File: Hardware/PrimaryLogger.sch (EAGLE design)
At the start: 72 parts, among them J1 CONN_42.54_SCREW, J2 CONN_42.54_SCREW, J3 CONN_42.54_SCREW, J4 CONN_42.54_SCREW, J5 CONN_32.54_SCREW, Q1 DMG3404, Q2 DMG3404, U1 MIC2005, U2 MIC2005, U25 SN74AUP3G34DCU, U3 TPL5010DDC, U4 TXS0102DCU, U5 SN74LVC1G3157SC70, U6 TCS3400, U7 SHTC3DFN, U8 MCP23008QFN, U9 MCP7940SOIC

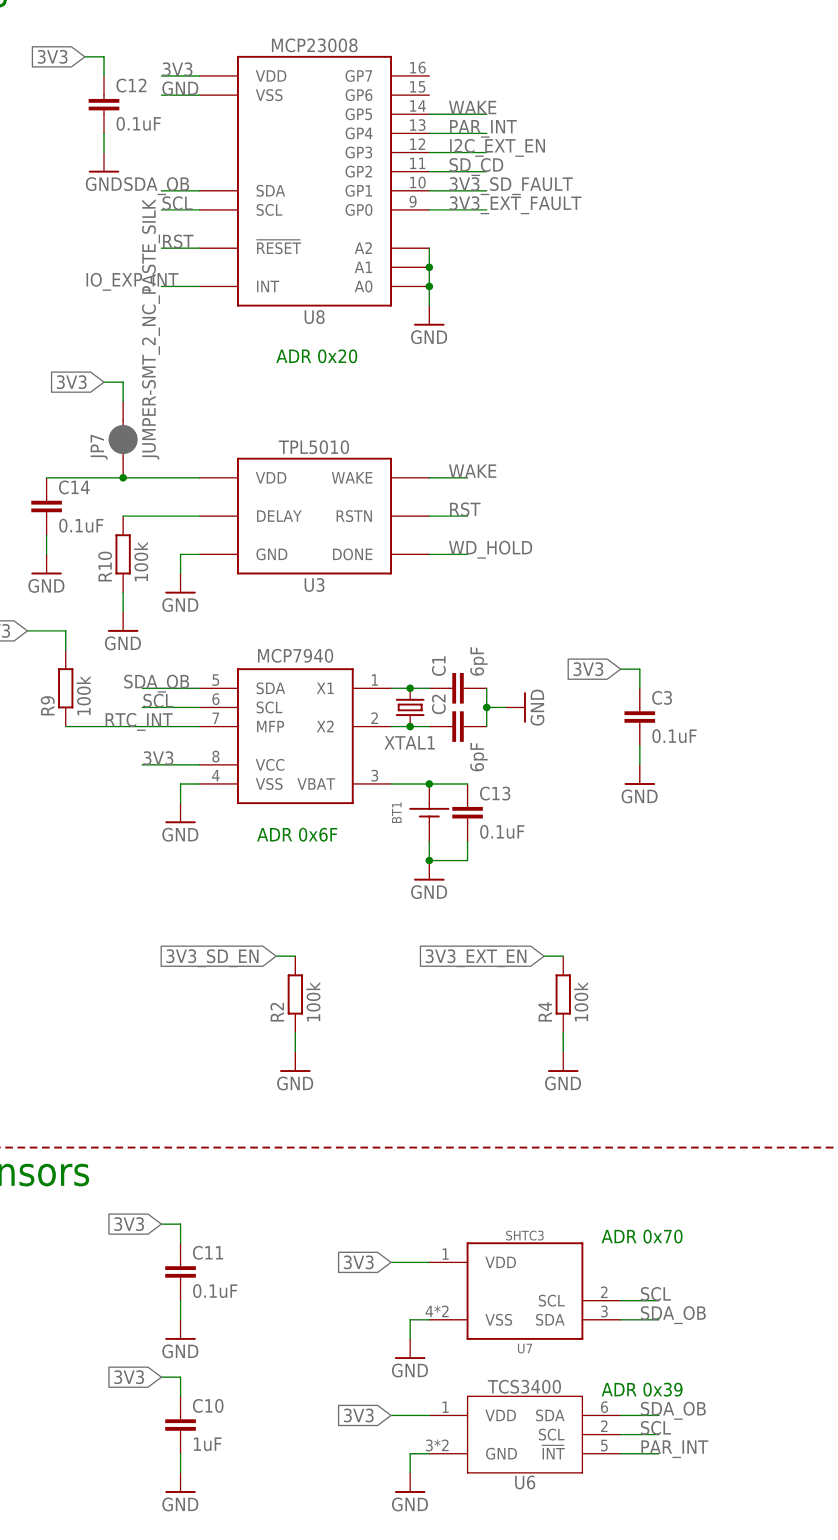
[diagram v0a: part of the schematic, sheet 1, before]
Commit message: Documentation and folder structure updates
Moved around the folder structure, added board pictures, and added to README
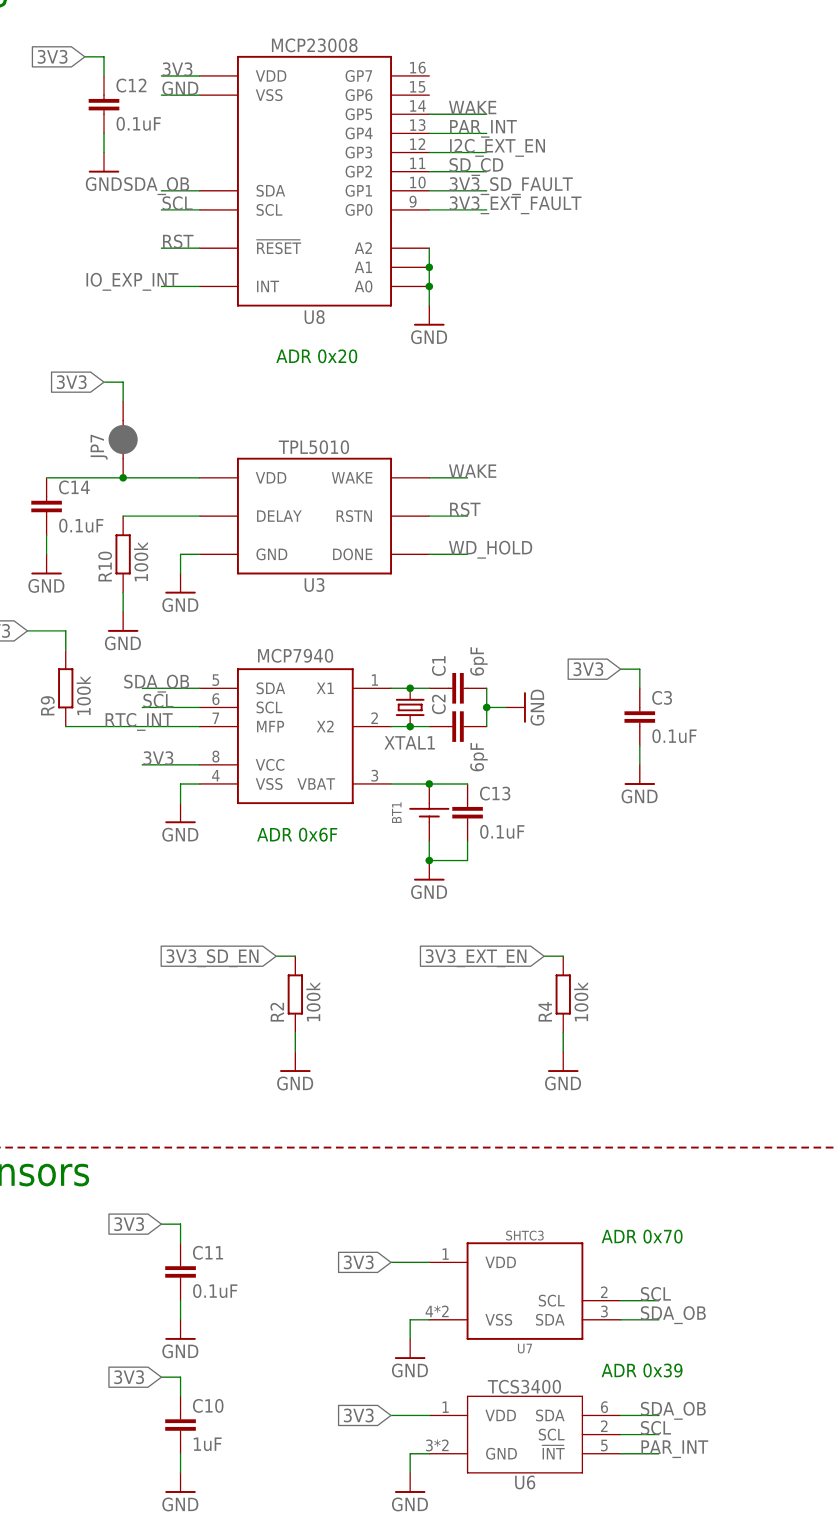
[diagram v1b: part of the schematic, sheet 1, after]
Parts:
- JP1, JP2, JP3, JP4, JP5, JP6, JP8: device bschulz:JUMPER-SMT_3_1-NC_PASTE_SILK -> SparkFun-Jumpers:JUMPER-SMT_3_1-NC_PASTE_SILK
- JP10: device bschulz:JUMPER-SMT_2_NO_SILK -> SparkFun-Jumpers:JUMPER-SMT_2_NO_SILK
- JP7, JP9: device bschulz:JUMPER-SMT_2_NC_PASTE_SILK -> SparkFun-Jumpers:JUMPER-SMT_2_NC_PASTE_SILK
- R8: value 10k -> 100k
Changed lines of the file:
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@@
 <?xml version="1.0" encoding="utf-8"?>
 <!DOCTYPE eagle SYSTEM "eagle.dtd">
-<eagle version="9.5.2">
+<eagle version="9.6.2">
 <drawing>
 <settings>
@@
 <layer number="115" name="ReferenceISLANDS" color="7" fill="1" visible="no" active="yes"/>
 <layer number="116" name="Patch_BOT" color="7" fill="1" visible="no" active="yes"/>
-<layer number="117" name="PM_Ref" color="7" fill="1" visible="no" active="no"/>
 <layer number="118" name="Rect_Pads" color="7" fill="1" visible="no" active="yes"/>
-<layer number="119" name="PF_Ref" color="7" fill="1" visible="no" active="no"/>
-<layer number="120" name="WFL_Ref" color="7" fill="1" visible="no" active="no"/>
 <layer number="121" name="_tsilk" color="7" fill="1" visible="no" active="yes"/>
 <layer number="122" name="_bsilk" color="7" fill="1" visible="no" active="yes"/>
@@
 <part name="J3" library="bschulz" deviceset="CONN_4" device="2.54_SCREW"/>
 <part name="J4" library="bschulz" deviceset="CONN_4" device="2.54_SCREW"/>
-<part name="JP1" library="bschulz" deviceset="JUMPER-SMT_3_1-NC_PASTE" device="_SILK" package3d_urn="urn:adsk.eagle:package:39293/1"/>
-<part name="JP2" library="bschulz" deviceset="JUMPER-SMT_3_1-NC_PASTE" device="_SILK" package3d_urn="urn:adsk.eagle:package:39293/1"/>
-<part name="JP3" library="bschulz" deviceset="JUMPER-SMT_3_1-NC_PASTE" device="_SILK" package3d_urn="urn:adsk.eagle:package:39293/1"/>
-<part name="JP4" library="bschulz" deviceset="JUMPER-SMT_3_1-NC_PASTE" device="_SILK" package3d_urn="urn:adsk.eagle:package:39293/1"/>
-<part name="JP5" library="bschulz" deviceset="JUMPER-SMT_3_1-NC_PASTE" device="_SILK" package3d_urn="urn:adsk.eagle:package:39293/1"/>
-<part name="JP6" library="bschulz" deviceset="JUMPER-SMT_3_1-NC_PASTE" device="_SILK" package3d_urn="urn:adsk.eagle:package:39293/1"/>
+<part name="JP1" library="SparkFun-Jumpers" library_urn="urn:adsk.eagle:library:528" deviceset="JUMPER-SMT_3_1-NC_PASTE" device="_SILK" package3d_urn="urn:adsk.eagle:package:39293/1"/>
+<part name="JP2" library="SparkFun-Jumpers" library_urn="urn:adsk.eagle:library:528" deviceset="JUMPER-SMT_3_1-NC_PASTE" device="_SILK" package3d_urn="urn:adsk.eagle:package:39293/1"/>
+<part name="JP3" library="SparkFun-Jumpers" library_urn="urn:adsk.eagle:library:528" deviceset="JUMPER-SMT_3_1-NC_PASTE" device="_SILK" package3d_urn="urn:adsk.eagle:package:39293/1"/>
+<part name="JP4" library="SparkFun-Jumpers" library_urn="urn:adsk.eagle:library:528" deviceset="JUMPER-SMT_3_1-NC_PASTE" device="_SILK" package3d_urn="urn:adsk.eagle:package:39293/1"/>
+<part name="JP5" library="SparkFun-Jumpers" library_urn="urn:adsk.eagle:library:528" deviceset="JUMPER-SMT_3_1-NC_PASTE" device="_SILK" package3d_urn="urn:adsk.eagle:package:39293/1"/>
+<part name="JP6" library="SparkFun-Jumpers" library_urn="urn:adsk.eagle:library:528" deviceset="JUMPER-SMT_3_1-NC_PASTE" device="_SILK" package3d_urn="urn:adsk.eagle:package:39293/1"/>
 <part name="U5" library="bschulz" deviceset="SN74LVC1G3157" device="SC70" value="SN74LVC1G3157SC70"/>
 <part name="R6" library="bschulz_passives" deviceset="R-EU_" device="R0603" technology="100K" value="100k"/>
@@
 <part name="J5" library="bschulz" deviceset="CONN_3" device="2.54_SCREW"/>
 <part name="J6" library="bschulz" deviceset="CONN_02" device="2.54_SCREW_ROUND"/>
-<part name="R8" library="bschulz_passives" deviceset="R-EU_" device="R0603" technology="10K" value="10k"/>
+<part name="R8" library="bschulz_passives" deviceset="R-EU_" device="R0603" technology="10K" value="100k"/>
 <part name="J7" library="bschulz" deviceset="CONN_02" device="3.5MM_ROUND"/>
 <part name="J8" library="bschulz" deviceset="CONN_02" device="3.5MM_ROUND"/>
@@
 </part>
 <part name="C14" library="bschulz_passives" deviceset="C-EU" device="C0603" technology="0.1UF" value="0.1uF"/>
-<part name="JP7" library="bschulz" deviceset="JUMPER-SMT_2_NC_PASTE" device="_SILK" package3d_urn="urn:adsk.eagle:package:39282/1"/>
+<part name="JP7" library="SparkFun-Jumpers" library_urn="urn:adsk.eagle:library:528" deviceset="JUMPER-SMT_2_NC_PASTE" device="_SILK" package3d_urn="urn:adsk.eagle:package:39282/1"/>
 <part name="GND23" library="supply1" library_urn="urn:adsk.eagle:library:371" deviceset="GND" device=""/>
 <part name="R9" library="bschulz_passives" deviceset="R-EU_" device="R0603" technology="100K" value="100k"/>
-<part name="JP8" library="bschulz" deviceset="JUMPER-SMT_3_1-NC_PASTE" device="_SILK" package3d_urn="urn:adsk.eagle:package:39293/1"/>
+<part name="JP8" library="SparkFun-Jumpers" library_urn="urn:adsk.eagle:library:528" deviceset="JUMPER-SMT_3_1-NC_PASTE" device="_SILK" package3d_urn="urn:adsk.eagle:package:39293/1"/>
 <part name="R11" library="bschulz_passives" deviceset="R-EU_" device="R0603" technology="100K" value="100k"/>
-<part name="JP9" library="bschulz" deviceset="JUMPER-SMT_2_NC_PASTE" device="_SILK" package3d_urn="urn:adsk.eagle:package:39282/1"/>
-<part name="JP10" library="bschulz" deviceset="JUMPER-SMT_2_NO" device="_SILK" package3d_urn="urn:adsk.eagle:package:39279/1"/>
+<part name="JP9" library="SparkFun-Jumpers" library_urn="urn:adsk.eagle:library:528" deviceset="JUMPER-SMT_2_NC_PASTE" device="_SILK" package3d_urn="urn:adsk.eagle:package:39282/1"/>
+<part name="JP10" library="SparkFun-Jumpers" library_urn="urn:adsk.eagle:library:528" deviceset="JUMPER-SMT_2_NO" device="_SILK" package3d_urn="urn:adsk.eagle:package:39279/1"/>
 </parts>
 <sheets>
@@
 <text x="7.62" y="45.72" size="3.81" layer="91">Sensors</text>
 <text x="144.78" y="203.2" size="3.81" layer="91">Power</text>
-<text x="93.98" y="17.78" size="1.778" layer="91">ADR 0x39</text>
+<text x="93.98" y="20.32" size="1.778" layer="91">ADR 0x39</text>
 <text x="93.98" y="38.1" size="1.778" layer="91">ADR 0x70</text>
 <text x="48.26" y="91.44" size="1.778" layer="91">ADR 0x6F</text>
@@
 <instance part="JP7" gate="G$1" x="30.48" y="144.78" smashed="yes" rot="R90">
 <attribute name="NAME" x="27.94" y="142.24" size="1.778" layer="95" font="vector" rot="R90"/>
-<attribute name="VALUE" x="33.02" y="142.24" size="1.778" layer="96" font="vector" rot="R90" align="top-left"/>
 </instance>
 <instance part="GND23" gate="1" x="20.32" y="127" smashed="yes">

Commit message: Further documentation updates
Moved production files around, updated BoM in hardware and part libraries links to support that (DNP values issue)
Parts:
- JP1, JP2, JP3, JP4, JP5, JP6, JP8: device SparkFun-Jumpers:JUMPER-SMT_3_1-NC_PASTE_SILK -> bschulz:JUMPER-SMT_3_1-NC_PASTE_SILK
- JP10: device SparkFun-Jumpers:JUMPER-SMT_2_NO_SILK -> bschulz:JUMPER-SMT_2_NO_SILK
- JP9: device SparkFun-Jumpers:JUMPER-SMT_2_NC_PASTE_SILK -> bschulz:JUMPER-SMT_2_NC_PASTE_SILK
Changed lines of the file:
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@@
 <layer number="115" name="ReferenceISLANDS" color="7" fill="1" visible="no" active="yes"/>
 <layer number="116" name="Patch_BOT" color="7" fill="1" visible="no" active="yes"/>
+<layer number="117" name="PM_Ref" color="7" fill="1" visible="no" active="no"/>
 <layer number="118" name="Rect_Pads" color="7" fill="1" visible="no" active="yes"/>
+<layer number="119" name="PF_Ref" color="7" fill="1" visible="no" active="no"/>
+<layer number="120" name="WFL_Ref" color="7" fill="1" visible="no" active="no"/>
 <layer number="121" name="_tsilk" color="7" fill="1" visible="no" active="yes"/>
 <layer number="122" name="_bsilk" color="7" fill="1" visible="no" active="yes"/>
@@
 <part name="J3" library="bschulz" deviceset="CONN_4" device="2.54_SCREW"/>
 <part name="J4" library="bschulz" deviceset="CONN_4" device="2.54_SCREW"/>
-<part name="JP1" library="SparkFun-Jumpers" library_urn="urn:adsk.eagle:library:528" deviceset="JUMPER-SMT_3_1-NC_PASTE" device="_SILK" package3d_urn="urn:adsk.eagle:package:39293/1"/>
-<part name="JP2" library="SparkFun-Jumpers" library_urn="urn:adsk.eagle:library:528" deviceset="JUMPER-SMT_3_1-NC_PASTE" device="_SILK" package3d_urn="urn:adsk.eagle:package:39293/1"/>
-<part name="JP3" library="SparkFun-Jumpers" library_urn="urn:adsk.eagle:library:528" deviceset="JUMPER-SMT_3_1-NC_PASTE" device="_SILK" package3d_urn="urn:adsk.eagle:package:39293/1"/>
-<part name="JP4" library="SparkFun-Jumpers" library_urn="urn:adsk.eagle:library:528" deviceset="JUMPER-SMT_3_1-NC_PASTE" device="_SILK" package3d_urn="urn:adsk.eagle:package:39293/1"/>
-<part name="JP5" library="SparkFun-Jumpers" library_urn="urn:adsk.eagle:library:528" deviceset="JUMPER-SMT_3_1-NC_PASTE" device="_SILK" package3d_urn="urn:adsk.eagle:package:39293/1"/>
-<part name="JP6" library="SparkFun-Jumpers" library_urn="urn:adsk.eagle:library:528" deviceset="JUMPER-SMT_3_1-NC_PASTE" device="_SILK" package3d_urn="urn:adsk.eagle:package:39293/1"/>
+<part name="JP1" library="bschulz" deviceset="JUMPER-SMT_3_1-NC_PASTE" device="_SILK" package3d_urn="urn:adsk.eagle:package:39293/1"/>
+<part name="JP2" library="bschulz" deviceset="JUMPER-SMT_3_1-NC_PASTE" device="_SILK" package3d_urn="urn:adsk.eagle:package:39293/1"/>
+<part name="JP3" library="bschulz" deviceset="JUMPER-SMT_3_1-NC_PASTE" device="_SILK" package3d_urn="urn:adsk.eagle:package:39293/1"/>
+<part name="JP4" library="bschulz" deviceset="JUMPER-SMT_3_1-NC_PASTE" device="_SILK" package3d_urn="urn:adsk.eagle:package:39293/1"/>
+<part name="JP5" library="bschulz" deviceset="JUMPER-SMT_3_1-NC_PASTE" device="_SILK" package3d_urn="urn:adsk.eagle:package:39293/1"/>
+<part name="JP6" library="bschulz" deviceset="JUMPER-SMT_3_1-NC_PASTE" device="_SILK" package3d_urn="urn:adsk.eagle:package:39293/1"/>
 <part name="U5" library="bschulz" deviceset="SN74LVC1G3157" device="SC70" value="SN74LVC1G3157SC70"/>
 <part name="R6" library="bschulz_passives" deviceset="R-EU_" device="R0603" technology="100K" value="100k"/>
@@
 <part name="GND23" library="supply1" library_urn="urn:adsk.eagle:library:371" deviceset="GND" device=""/>
 <part name="R9" library="bschulz_passives" deviceset="R-EU_" device="R0603" technology="100K" value="100k"/>
-<part name="JP8" library="SparkFun-Jumpers" library_urn="urn:adsk.eagle:library:528" deviceset="JUMPER-SMT_3_1-NC_PASTE" device="_SILK" package3d_urn="urn:adsk.eagle:package:39293/1"/>
+<part name="JP8" library="bschulz" deviceset="JUMPER-SMT_3_1-NC_PASTE" device="_SILK" package3d_urn="urn:adsk.eagle:package:39293/1"/>
 <part name="R11" library="bschulz_passives" deviceset="R-EU_" device="R0603" technology="100K" value="100k"/>
-<part name="JP9" library="SparkFun-Jumpers" library_urn="urn:adsk.eagle:library:528" deviceset="JUMPER-SMT_2_NC_PASTE" device="_SILK" package3d_urn="urn:adsk.eagle:package:39282/1"/>
-<part name="JP10" library="SparkFun-Jumpers" library_urn="urn:adsk.eagle:library:528" deviceset="JUMPER-SMT_2_NO" device="_SILK" package3d_urn="urn:adsk.eagle:package:39279/1"/>
+<part name="JP9" library="bschulz" deviceset="JUMPER-SMT_2_NC_PASTE" device="_SILK" package3d_urn="urn:adsk.eagle:package:39282/1"/>
+<part name="JP10" library="bschulz" deviceset="JUMPER-SMT_2_NO" device="_SILK" package3d_urn="urn:adsk.eagle:package:39279/1"/>
 </parts>
 <sheets>

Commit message: Cleaned up schematic and made new PDF - final v0.2
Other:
- note added: "DNP for production"
- note removed: "Remove for production!"
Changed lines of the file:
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@@
 <part name="JP9" library="bschulz" deviceset="JUMPER-SMT_2_NC_PASTE" device="_SILK" package3d_urn="urn:adsk.eagle:package:39282/1"/>
 <part name="JP10" library="bschulz" deviceset="JUMPER-SMT_2_NO" device="_SILK" package3d_urn="urn:adsk.eagle:package:39279/1"/>
+<part name="GND24" library="supply1" library_urn="urn:adsk.eagle:library:371" deviceset="GND" device=""/>
 </parts>
 <sheets>
@@
 <segment>
 <pinref part="U1" gate="G$1" pin="EN"/>
-<wire x1="198.12" y1="152.4" x2="193.04" y2="152.4" width="0.1524" layer="91"/>
-<label x="193.04" y="152.4" size="0.6096" layer="95" rot="R180" xref="yes"/>
+<wire x1="198.12" y1="152.4" x2="195.58" y2="152.4" width="0.1524" layer="91"/>
+<label x="195.58" y="152.4" size="0.6096" layer="95" rot="R180" xref="yes"/>
 </segment>
 <segment>
@@
 <segment>
 <pinref part="U2" gate="G$1" pin="EN"/>
-<wire x1="198.12" y1="177.8" x2="193.04" y2="177.8" width="0.1524" layer="91"/>
-<label x="193.04" y="177.8" size="0.6096" layer="95" rot="R180" xref="yes"/>
+<wire x1="198.12" y1="177.8" x2="195.58" y2="177.8" width="0.1524" layer="91"/>
+<label x="195.58" y="177.8" size="0.6096" layer="95" rot="R180" xref="yes"/>
 </segment>
 <segment>
@@
 <text x="109.22" y="20.32" size="0.6096" layer="91" align="top-left">Note:
 Must be 3v3, NOT 3V3_EXT, since tips are asynchronous</text>
-<text x="10.16" y="86.36" size="2.54" layer="91">Remove for production!</text>
+<text x="5.08" y="86.36" size="2.54" layer="91">DNP for production</text>
 <text x="66.04" y="180.34" size="1.778" layer="91">Flex - A</text>
 <text x="66.04" y="177.8" size="1.778" layer="91">Flex - A</text>
@@
 <attribute name="NAME" x="147.32" y="63.5" size="1.778" layer="95" font="vector" rot="R180"/>
 </instance>
+<instance part="GND24" gate="1" x="104.14" y="7.62" smashed="yes">
+<attribute name="VALUE" x="101.6" y="5.08" size="1.778" layer="96"/>
+</instance>
 </instances>
 <busses>
@@
 <pinref part="J6" gate="G$1" pin="2"/>
 <wire x1="109.22" y1="12.7" x2="104.14" y2="12.7" width="0.1524" layer="91"/>
-<label x="101.6" y="12.7" size="1.778" layer="95"/>
+<pinref part="GND24" gate="1" pin="GND"/>
+<wire x1="104.14" y1="10.16" x2="104.14" y2="12.7" width="0.1524" layer="91"/>
 </segment>
 <segment>
@@
 <pinref part="R8" gate="G$1" pin="1"/>
 <wire x1="104.14" y1="25.4" x2="104.14" y2="27.94" width="0.1524" layer="91"/>
-<wire x1="104.14" y1="27.94" x2="99.06" y2="27.94" width="0.1524" layer="91"/>
-<label x="99.06" y="27.94" size="1.778" layer="95"/>
+<wire x1="104.14" y1="27.94" x2="101.6" y2="27.94" width="0.1524" layer="91"/>
+<label x="101.6" y="27.94" size="1.778" layer="95" rot="R180" xref="yes"/>
 </segment>
 <segment>
@@
 <pinref part="J6" gate="G$1" pin="1"/>
 <wire x1="109.22" y1="15.24" x2="104.14" y2="15.24" width="0.1524" layer="91"/>
-<label x="99.06" y="15.24" size="1.778" layer="95"/>
 <pinref part="R8" gate="G$1" pin="2"/>
 <wire x1="104.14" y1="15.24" x2="99.06" y2="15.24" width="0.1524" layer="91"/>
 <junction x="104.14" y="15.24"/>
-</segment>
-<segment>
+<label x="99.06" y="15.24" size="1.778" layer="95" rot="R180" xref="yes"/>
+</segment>
+<segment>
